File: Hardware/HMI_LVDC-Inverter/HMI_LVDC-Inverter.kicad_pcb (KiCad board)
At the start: 2 copper layers, 83.6 x 76 mm, 137 parts, among them J1 Micro_PwrBus_B1, J10 Inv_Signal2_A1, J11 Conn_01x04_Pin, J2 Conn_01x06_Pin, J3 Screw_Terminal_01x08, J4 Screw_Terminal_01x03, J5 Conn_01x02, J7 Inverter_MEAS, J8 Inv_Signal1_A1, J9 ESP32_Programmer, K1 RT174012, Q1 BC847, Q2 2N7002, SW1 SolderJumper_2_Open, SW2 SW_MEC_5G, SW3 SW_MEC_5G, SW4 SW_MEC_5G, SW5 SW_MEC_5G, SW6 SW_MEC_5G, SW7 SW_MEC_5G, SW8 SW_MEC_5G, SW9 SW_MEC_5G, U1 STM32F103C8Tx, U10 MCP23017_SO, U11 4N25, U12 4N25, U13 4N25, U14 4N25, U15 4N25, U16 4N25, U2 ESP32-WROOM-32E-N16, U3 AMS1117-3.3, U4 B1205S-2WR2, U5 AMS1117-3.3, U6 B1205S-2WR2, U7 4N25, U8 4N25, U9 PC817, Y1 Crystal 8MHz, Y2 32.768KHz

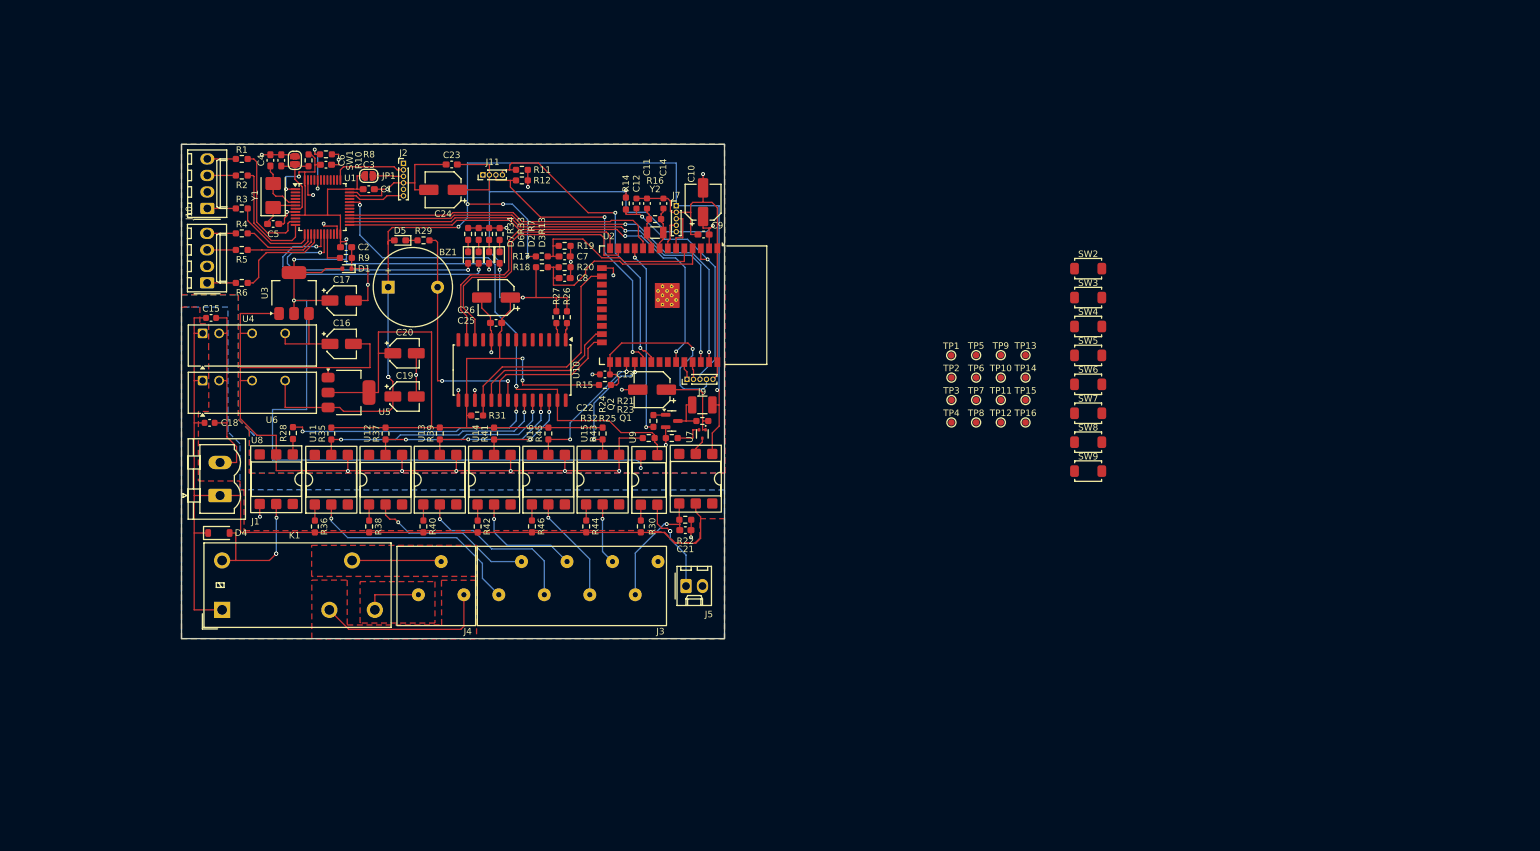
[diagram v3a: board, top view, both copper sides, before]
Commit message: Terminada la placa del HMI con revisión de reglas de diseño
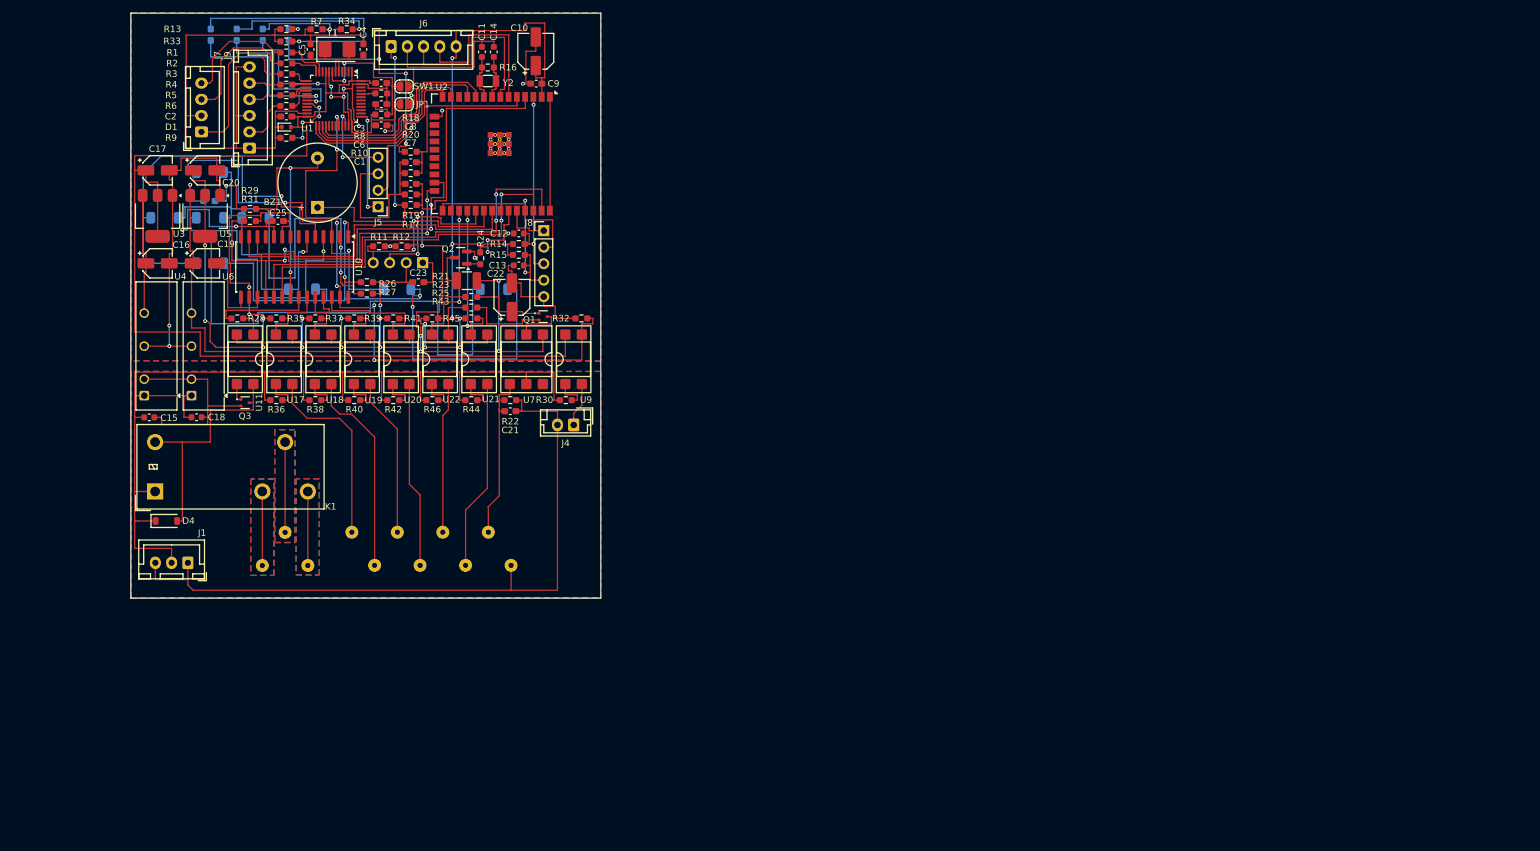
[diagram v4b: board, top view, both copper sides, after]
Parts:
- removed C24, C26: 22uF, Capacitor_SMD:CP_Elec_5x5.4
- removed J11: Conn_01x04_Pin, Connector_PinHeader_1.00mm:PinHeader_1x04_P1.00mm_Vertical
- removed the J2 at (94.8, 38.6)
- removed TP1, TP10, TP11, TP12, TP13, TP14, TP15, TP16, TP2, TP3, TP4, TP5, TP6, TP7, TP8, TP9: TestPoint, TestPoint:TestPoint_Pad_D1.0mm
- removed U12, U13, U14, U15, U16, U8: 4N25, Package_DIP:DIP-6_W7.62mm_SMDSocket_SmallPads
- added J5: Inv_Signal1_A1, Connector_PinHeader_2.54mm:PinHeader_1x04_P2.54mm_Vertical, F.Cu at (90.9, 45.3)
- added J9: Conn_01x06, Connector_JST:JST_XH_B6B-XH-A_1x06_P2.50mm_Vertical, F.Cu at (71.1, 36.3)
- added Q3: BC847, Package_TO_SOT_SMD:SOT-523, F.Cu at (70.4, 75.5)
- added U17: PC817, Package_DIP:DIP-4_W7.62mm_SMDSocket_SmallPads, F.Cu at (76.4, 68.8)
- added U18: PC817, Package_DIP:DIP-4_W7.62mm_SMDSocket_SmallPads, F.Cu at (82.4, 68.8)
- added U19: PC817, Package_DIP:DIP-4_W7.62mm_SMDSocket_SmallPads, F.Cu at (88.4, 68.8)
- added U20: PC817, Package_DIP:DIP-4_W7.62mm_SMDSocket_SmallPads, F.Cu at (94.4, 68.8)
- added U21: PC817, Package_DIP:DIP-4_W7.62mm_SMDSocket_SmallPads, F.Cu at (106.4, 68.8)
- added U22: PC817, Package_DIP:DIP-4_W7.62mm_SMDSocket_SmallPads, F.Cu at (100.4, 68.8)
- D2, D3, D5, D6, D7, J3, SW2, SW3, SW4, SW5, SW6, SW7, SW8, SW9: moved to B.Cu
- J1: footprint Connector_Phoenix_MSTB:PhoenixContact_MSTBVA_2,5_2-G-5,08_1x02_P5.08mm_Vertical -> Connector_JST:JST_XH_B3B-XH-A_1x03_P2.50mm_Vertical
- J10: value Inv_Signal2_A1 -> OLED; footprint Connector_Molex:Molex_KK-254_AE-6410-04A_1x04_P2.54mm_Vertical -> Footprints:Display OLED; moved to B.Cu
- J2: renamed from J4; moved to B.Cu
- J4: renamed from J5; footprint Connector_Molex:Molex_KK-254_AE-6410-02A_1x02_P2.54mm_Vertical -> Connector_JST:JST_EH_B2B-EH-A_1x02_P2.50mm_Vertical
- J6: renamed from J7; footprint Connector_PinHeader_1.00mm:PinHeader_1x05_P1.00mm_Vertical -> Connector_JST:JST_XH_B5B-XH-A_1x05_P2.50mm_Vertical
- J7: renamed from J8; footprint Connector_Molex:Molex_KK-254_AE-6410-04A_1x04_P2.54mm_Vertical -> Connector_JST:JST_XH_B4B-XH-A_1x04_P2.50mm_Vertical
- J8: renamed from J9; footprint Connector_PinHeader_1.00mm:PinHeader_1x05_P1.00mm_Vertical -> Connector_PinHeader_2.54mm:PinHeader_1x05_P2.54mm_Vertical
- U11: value 4N25 -> PC817; footprint Package_DIP:DIP-6_W7.62mm_SMDSocket_SmallPads -> Package_DIP:DIP-4_W7.62mm_SMDSocket_SmallPads
- U2: footprint RF_Module:ESP32-WROOM-32D -> RF_Module:ESP32-WROOM-32E
- moved SW8 146.3 mm to (58.0, 47.0), turned to 180 degrees
- moved SW6 139.0 mm to (65.0, 40.0), turned to 180 degrees
- moved SW7 138.4 mm to (65.0, 47.0), turned to 180 degrees
- moved SW4 135.5 mm to (65.0, 54.0), turned to 180 degrees
- moved SW9 133.9 mm to (72.0, 47.0), turned to 180 degrees
- moved SW5 121.4 mm to (79.1, 58.0), turned to 180 degrees
- moved SW2 106.4 mm to (93.8, 58.0), turned to 180 degrees
- moved SW3 91.4 mm to (108.7, 58.0), turned to 180 degrees
- moved D6 53.6 mm to (65.1, 18.8)
- moved J6 50.3 mm to (92.9, 20.6)
- moved D7 49.4 mm to (69.1, 18.8)
- moved D2 48.9 mm to (73.1, 18.8)
- moved D3 47.2 mm to (77.1, 18.8)
- moved R31 46.0 mm to (71.2, 47.5), turned to 180 degrees
- moved R13 45.5 mm to (76.8, 18.0), turned to 180 degrees
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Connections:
- J1 pad 1: +12V_ISO -> GND_ISO
- J1 pad 2: GND_ISO -> +12V_ISO
- J10 pad 1: /STM32/W_Sd -> GND
- J10 pad 2: GND -> +3.3V_ESP
- J10 pad 3: /STM32/W_In -> /ESP32/OLED_SCL
- J10 pad 4: /STM32/V_Sd -> /ESP32/OLED_SDA
- J3 pad 1: /Perifericos/FREQ_SEL_1_ISO -> GND_ISO
- J3 pad 2: /Perifericos/FREQ_SEL_2_ISO -> /Perifericos/0_10V_ISO
- J3 pad 3: /Perifericos/FREQ_SEL_3_ISO -> /Perifericos/START_CTRL_ISO
- J3 pad 4: /Perifericos/FREQ_SEL_4_ISO -> /Perifericos/STOP_BUTTON_ISO
- J3 pad 5: /Perifericos/STOP_BUTTON_ISO -> /Perifericos/FREQ_SEL_4_ISO
- J3 pad 6: /Perifericos/START_CTRL_ISO -> /Perifericos/FREQ_SEL_3_ISO
- J3 pad 7: /Perifericos/0_10V_ISO -> /Perifericos/FREQ_SEL_2_ISO
- J3 pad 8: GND_ISO -> /Perifericos/FREQ_SEL_1_ISO
- U11 pad 1: Net-(R36-Pad1) -> Net-(R28-Pad2)
- U11 pad 2: /Perifericos/FREQ_SEL_1_ISO -> GND
- U11 pad 3: unconnected-(U11-NC-Pad3) -> Net-(Q3-B)
- U11 pad 4: GND -> Net-(D4-A)
- U2 pad 11: /ESP32/V0-10V -> /ESP32/MISO
- U2 pad 13: /ESP32/SCL_MCP -> /ESP32/SCK
- U2 pad 14: /ESP32/SDA_MCP -> /ESP32/NSS
- U2 pad 16: /ESP32/RESET_MCP -> unconnected-(U2-IO13-Pad16)
- U2 pad 23: /ESP32/INT_B -> /ESP32/SCL_MCP
- U2 pad 24: /ESP32/INT_A -> /ESP32/SDA_MCP
- U2 pad 31: unconnected-(U2-IO19-Pad31) -> /ESP32/RESET_MCP
- U2 pad 33: /ESP32/NSS -> /ESP32/V0-10V
- U2 pad 36: /ESP32/SCK -> /ESP32/INT_A
- U2 pad 37: /ESP32/MISO -> /ESP32/INT_B
- U2 pad 4: /ESP32/3.3V_test -> /ESP32/5V_test
- U2 pad 5: /ESP32/5V_test -> /ESP32/3.3V_test
- U2 pad 6: /ESP32/VSens_Corriente -> /ESP32/Vsens_HV
- U2 pad 7: /ESP32/Vsens_HV -> /ESP32/VSens_Corriente
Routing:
- net /Perifericos/Matrix_3: track 0.00 -> 120.5 mm, vias 0 -> 1
- net GND_ISO: track 36.1 -> 141.7 mm, vias 2 -> 0
- net GND: track 290.6 -> 390.7 mm, vias 25 -> 15
- net /Perifericos/Matrix_0: track 2.64 -> 99.6 mm, vias 0 -> 4
- net /Perifericos/Matrix_1: track 2.63 -> 72.3 mm, vias 0 -> 2
- net +3.3V_ESP: track 232.4 -> 299.8 mm, vias 6 -> 23
- net /Perifericos/Matrix_4: track 0.00 -> 63.3 mm, vias 0 -> 1
- net /Perifericos/Matrix_2: track 0.00 -> 53.4 mm, vias 0 -> 2
- net /ESP32/SCK: track 72.2 -> 29.4 mm, vias 2 -> 0
- net /ESP32/MISO: track 73.2 -> 31.6 mm, vias 2 -> 0
- net /ESP32/NSS: track 70.0 -> 28.6 mm, vias 2 -> 0
- net Net-(D6-K): track 1.84 -> 39.7 mm, vias 0 -> 1
- net /ESP32/INT_B: track 23.6 -> 61.1 mm, vias 0 -> 2
- net /ESP32/INT_A: track 22.0 -> 56.9 mm, vias 0 -> 2
- net /Perifericos/Matrix_5: track 0.00 -> 29.1 mm, vias 0 -> 1
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- added copper zone on B.Cu, net /Perifericos/RELAY_COM
- added copper zone on B.Cu, net /Perifericos/RELAY_NC
- added copper zone on B.Cu, net /Perifericos/RELAY_NO
- added copper zone on F.Cu, net GND_ISO
- removed copper zone on F.Cu, net +12V_ISO
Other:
- board size 83.6 x 76 mm -> 72.3 x 90 mm

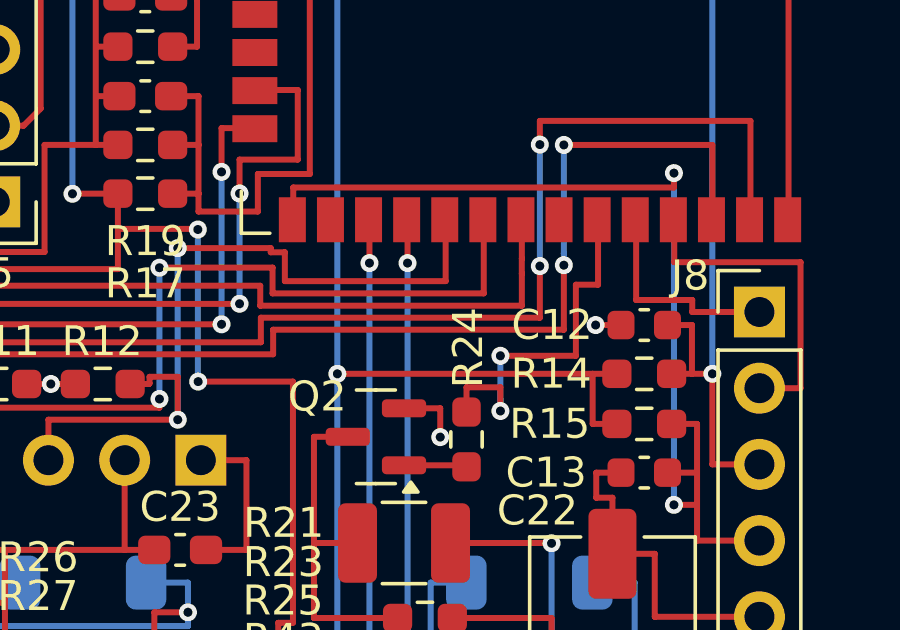
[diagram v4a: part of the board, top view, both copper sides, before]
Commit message: Cambio de pin de 0-10V
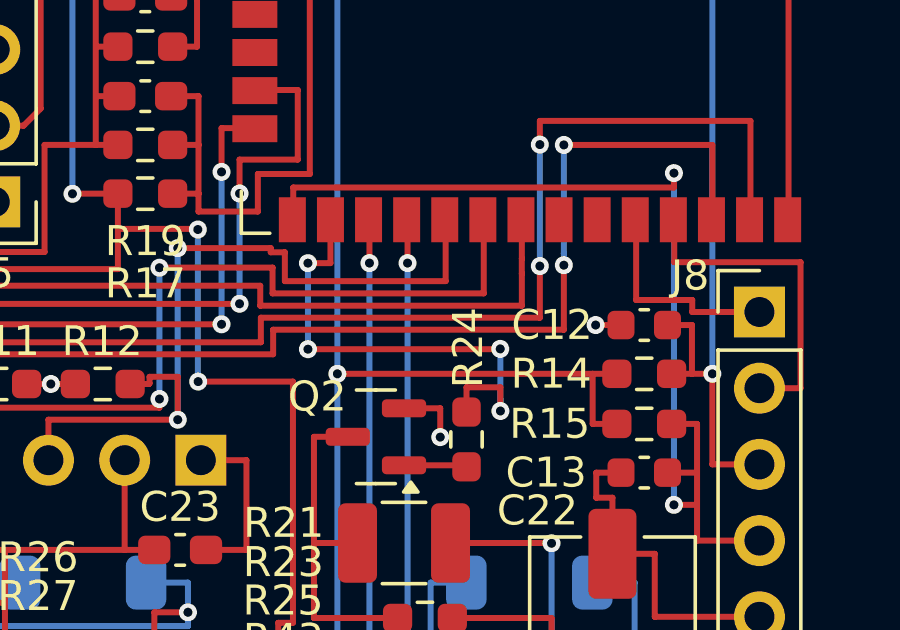
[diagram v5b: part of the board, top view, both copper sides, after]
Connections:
- U2 pad 26: unconnected-(U2-IO4-Pad26) -> /ESP32/V0-10V
- U2 pad 33: /ESP32/V0-10V -> unconnected-(U2-IO21-Pad33)
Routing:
- net /ESP32/V0-10V: track 12.8 -> 16.7 mm, vias 2 -> 4
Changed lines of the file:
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@@
 	(net 102 "unconnected-(U2-NC-Pad21)")
 	(net 103 "/ESP32/SDA_MCP")
-	(net 104 "unconnected-(U2-IO4-Pad26)")
+	(net 104 "unconnected-(U2-IO21-Pad33)")
 	(net 105 "unconnected-(U2-NC-Pad22)")
 	(net 106 "/ESP32/INT_B")
@@
 			(net 133 "unconnected-(U2-IO13-Pad16)")
 			(pinfunction "IO13")
-			(pintype "bidirectional")
+			(pintype "bidirectional+no_connect")
 		)
 		(pad "17" smd rect
@@
 			(size 1.5 0.9)
 			(layers "F.Cu" "F.Mask" "F.Paste")
-			(net 104 "unconnected-(U2-IO4-Pad26)")
+			(net 61 "/ESP32/V0-10V")
 			(pinfunction "IO4")
-			(pintype "bidirectional+no_connect")
+			(pintype "bidirectional")
 		)
 		(pad "27" smd rect
@@
 			(size 1.5 0.9)
 			(layers "F.Cu" "F.Mask" "F.Paste")
-			(net 61 "/ESP32/V0-10V")
+			(net 104 "unconnected-(U2-IO21-Pad33)")
 			(pinfunction "IO21")
-			(pintype "bidirectional")
+			(pintype "bidirectional+no_connect")
 		)
 		(pad "34" smd rect
@@
 	)
 	(segment
-		(start 107.73 50.44)
-		(end 110.246 50.44)
+		(start 107.715 50.22)
+		(end 101.315 50.22)
 		(width 0.2)
 		(layer "F.Cu")
@@
 	)
 	(segment
-		(start 110.985 48.07)
-		(end 110.985 45.88)
+		(start 101.315 47.351)
+		(end 102.065 47.351)
 		(width 0.2)
 		(layer "F.Cu")
@@
 	)
 	(segment
-		(start 110.246 50.44)
-		(end 110.246 48.07)
-		(width 0.2)
-		(layer "F.Cu")
-		(net 61)
-	)
-	(segment
-		(start 110.246 48.07)
-		(end 110.985 48.07)
+		(start 106.6 51.49)
+		(end 106.6 52.315)
 		(width 0.2)
 		(layer "F.Cu")
@@
 	)
 	(segment
-		(start 106.6 51.49)
-		(end 106.6 52.315)
+		(start 102.065 47.351)
+		(end 102.065 45.905)
 		(width 0.2)
 		(layer "F.Cu")
@@
 	)
 	(via
-		(at 107.73 50.44)
+		(at 101.315 50.22)
+		(size 0.6)
+		(drill 0.3)
+		(layers "F.Cu" "B.Cu")
+		(net 61)
+	)
+	(via
+		(at 101.315 47.351)
+		(size 0.6)
+		(drill 0.3)
+		(layers "F.Cu" "B.Cu")
+		(free yes)
+		(net 61)
+	)
+	(via
+		(at 107.725 50.21)
 		(size 0.6)
 		(drill 0.3)
@@
 	)
 	(segment
+		(start 107.73 50.295)
+		(end 107.73 52.28)
+		(width 0.2)
+		(layer "B.Cu")
+		(net 61)
+	)
+	(segment
 		(start 107.73 52.28)
 		(end 107.73 51.885)
@@
 	)
 	(segment
-		(start 107.73 50.44)
-		(end 107.73 52.28)
+		(start 101.315 50.22)
+		(end 101.315 47.351)
+		(width 0.2)
+		(layer "B.Cu")
+		(net 61)
+	)
+	(segment
+		(start 107.725 50.29)
+		(end 107.73 50.295)
+		(width 0.2)
+		(layer "B.Cu")
+		(net 61)
+	)
+	(segment
+		(start 107.725 50.21)
+		(end 107.725 50.29)
 		(width 0.2)
 		(layer "B.Cu")
